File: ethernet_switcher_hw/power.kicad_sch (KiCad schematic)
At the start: 1 part, among them IC1 LM2596S-ADJ

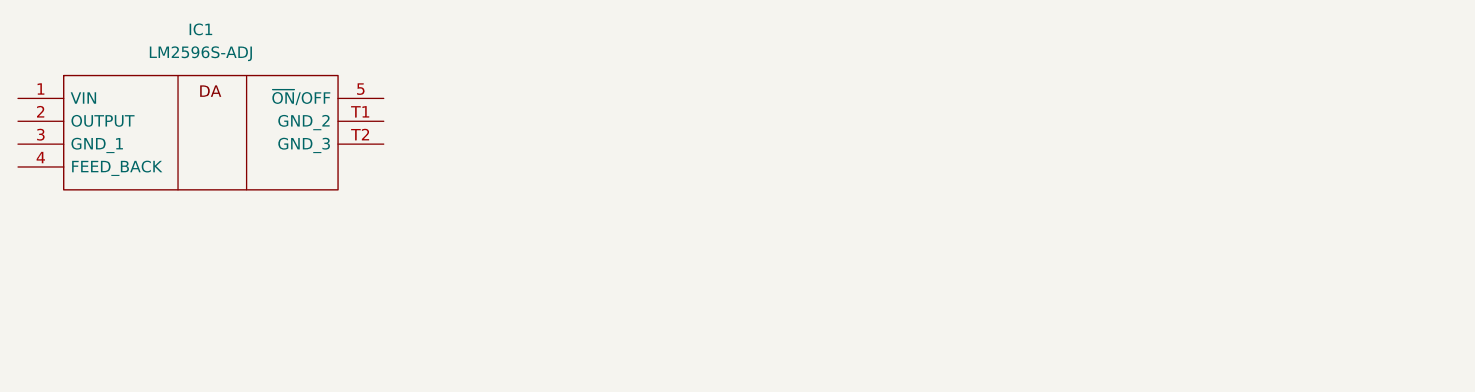
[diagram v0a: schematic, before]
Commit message: timer works incorrectly. It's clocked from slower source
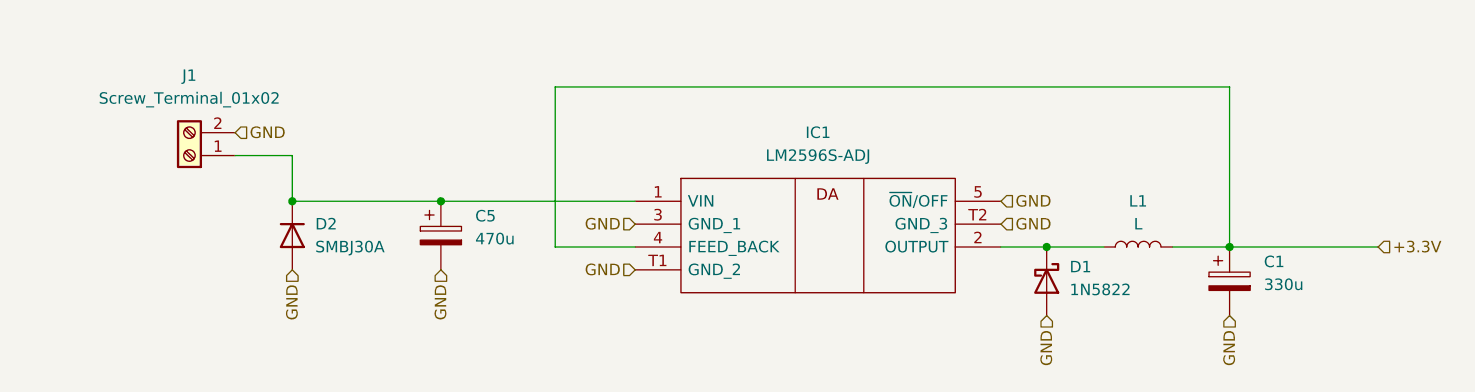
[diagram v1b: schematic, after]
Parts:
- added C1: 330u, Capacitor_THT:CP_Radial_D6.3mm_P2.50mm, symbol Device:C_Polarized
- added C5: 470u, Capacitor_THT:CP_Radial_D13.0mm_P5.00mm, symbol Device:C_Polarized
- added D1: 1N5822, Diode_THT:D_DO-201AD_P15.24mm_Horizontal, symbol Diode:1N5822
- added D2: SMBJ30A, Diode_SMD:D_SMB, symbol Device:D
- added J1: Screw_Terminal_01x02, symbol Connector:Screw_Terminal_01x02
- added L1: L, Inductor_SMD:L_TDK_SLF12565, symbol Device:L
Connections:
- net at IC1.1 (VIN): now also C5.1, D2.1 (K), J1.1 (Pin_1)
- net at IC1.2 (OUTPUT): now also D1.1 (K), L1.1
- net GND: now reaches IC1.3 (GND_1)
- net GND: now also IC1.5 (~{ON}/OFF), IC1.T1 (GND_2), IC1.T2 (GND_3), C1.2, C5.2, D1.2 (A), D2.2 (A), J1.2 (Pin_2)
- net +3.3V: now reaches IC1.4 (FEED_BACK)
- net +3.3V: now also C1.1, L1.2
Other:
- moved on the sheet: IC1
